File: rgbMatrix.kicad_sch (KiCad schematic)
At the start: 1 part, among them IC1 IS31FL3743A-QULS4-TR

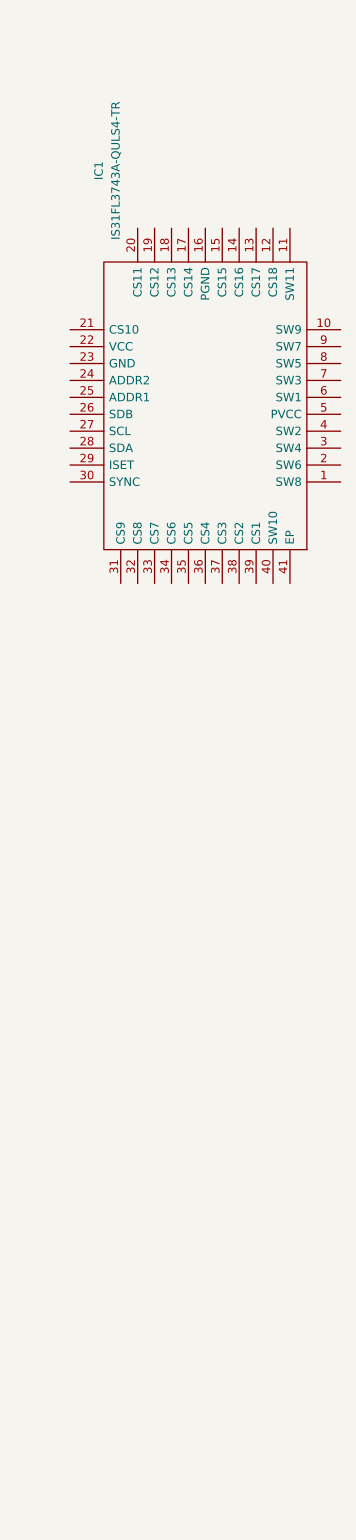
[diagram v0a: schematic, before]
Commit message: Started work on Led sch,
Decided on led driver IC
Decided on led part
started work on led matrix
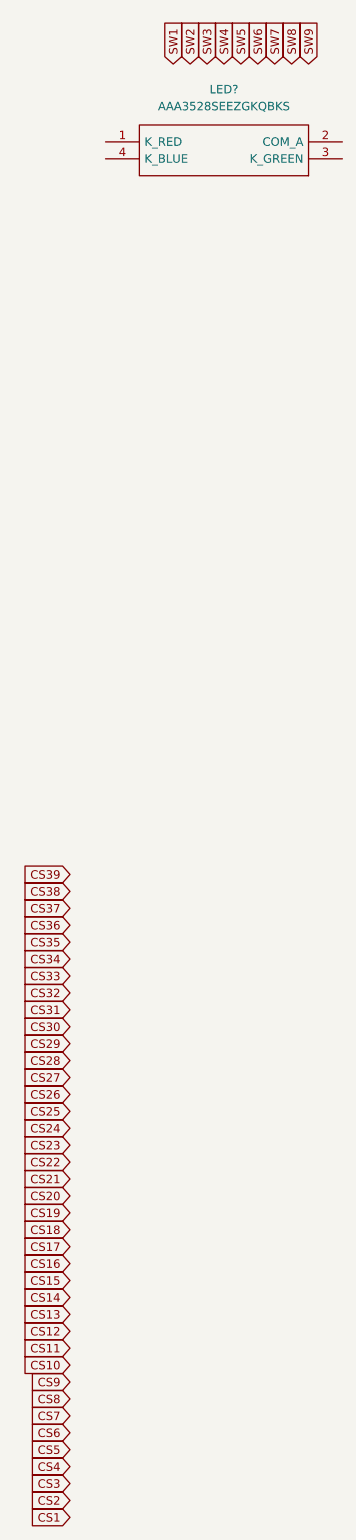
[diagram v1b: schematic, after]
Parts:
- removed IC1: IS31FL3743A-QULS4-TR, QFN40P500X500X60-41N-D, symbol IS31FL3743A-QULS4-TR:IS31FL3743A-QULS4-TR
- added LED?: AAA3528SEEZGKQBKS, AAA3528SEEZGKQBKS, symbol AAA3528SEEZGKQBKS:AAA3528SEEZGKQBKS

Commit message: Changed led driver
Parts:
- added D? (x108): D_Small, symbol Device:D_Small
- added LED? (x116): ESC, AAA3528SEEZGKQBKS, symbol AAA3528SEEZGKQBKS:AAA3528SEEZGKQBKS
- added R_B0, R_B12, R_B? (x11), R_G0, R_G12, R_G? (x11): 20, symbol Device:R_Small
- added R_R0, R_R12, R_R? (x11): 51, symbol Device:R_Small
- added SW?: W, symbol Switch:SW_Push
- added SW? (x3): SW_Push, symbol Switch:SW_Push
- added SW?: R_SHIFT, symbol Switch:SW_Push
- added SW?: 6, symbol Switch:SW_Push
- added SW?: ., symbol Switch:SW_Push
- added SW?: SCR_LK, symbol Switch:SW_Push
- added SW?: /, symbol Switch:SW_Push
- added SW?: X, symbol Switch:SW_Push
- added SW?: PAD_ENTER, symbol Switch:SW_Push
- added SW?: F9, symbol Switch:SW_Push
- added SW?: U, symbol Switch:SW_Push
- added SW?: BACKSPACE, symbol Switch:SW_Push
- added SW?: INSERT, symbol Switch:SW_Push
- added SW?: R_ARROW, symbol Switch:SW_Push
- added SW?: PAD_0, symbol Switch:SW_Push
- added SW?: F12, symbol Switch:SW_Push
- added SW?: 5, symbol Switch:SW_Push
- added SW?: CAPS, symbol Switch:SW_Push
- added SW?: T, symbol Switch:SW_Push
- added SW?: PAD_., symbol Switch:SW_Push
- added SW?: PG_UP, symbol Switch:SW_Push
- added SW?: 9, symbol Switch:SW_Push
- added SW?: ESC, symbol Switch:SW_Push
- added SW?: PAD_8, symbol Switch:SW_Push
- added SW?: F6, symbol Switch:SW_Push
- added SW?: PAD_2, symbol Switch:SW_Push
- added SW?: PAD_5, symbol Switch:SW_Push
- added SW?: +, symbol Switch:SW_Push
- added SW?: PAD_/, symbol Switch:SW_Push
- added SW?: 1, symbol Switch:SW_Push
- added SW?: F11, symbol Switch:SW_Push
- added SW?: I, symbol Switch:SW_Push
- added SW?: Z, symbol Switch:SW_Push
- added SW?: G, symbol Switch:SW_Push
- added SW?: \, symbol Switch:SW_Push
- added SW?: -, symbol Switch:SW_Push
- added SW?: 8, symbol Switch:SW_Push
- added SW?: PAD_BACK, symbol Switch:SW_Push
- added SW?: PAD_1, symbol Switch:SW_Push
- added SW?: E, symbol Switch:SW_Push
- added SW?: PG_DN, symbol Switch:SW_Push
- added SW?: END, symbol Switch:SW_Push
- added SW?: ', symbol Switch:SW_Push
- added SW?: P, symbol Switch:SW_Push
- added SW?: TILDE, symbol Switch:SW_Push
- added SW?: D, symbol Switch:SW_Push
- added SW?: PAD_9, symbol Switch:SW_Push
- added SW?: K, symbol Switch:SW_Push
- added SW?: PAD_3, symbol Switch:SW_Push
- added SW?: 0, symbol Switch:SW_Push
- added SW?: OS, symbol Switch:SW_Push
- added SW?: ENTER, symbol Switch:SW_Push
- added SW?: NUM_LK, symbol Switch:SW_Push
- added SW?: F8, symbol Switch:SW_Push
- added SW?: ], symbol Switch:SW_Push
- added SW?: ;, symbol Switch:SW_Push
- added SW?: =, symbol Switch:SW_Push
- added SW?: *, symbol Switch:SW_Push
- added SW?: F1, symbol Switch:SW_Push
- added SW?: C, symbol Switch:SW_Push
- added SW?: F10, symbol Switch:SW_Push
- added SW?: V, symbol Switch:SW_Push
- added SW?: F4, symbol Switch:SW_Push
- added SW?: PAUSE, symbol Switch:SW_Push
- added SW?: R_ALT, symbol Switch:SW_Push
- added SW?: CTRL, symbol Switch:SW_Push
- added SW?: FN, symbol Switch:SW_Push
- added SW?: 2, symbol Switch:SW_Push
- added SW?: A, symbol Switch:SW_Push
- added SW?: HOME, symbol Switch:SW_Push
- added SW?: R_CTRL, symbol Switch:SW_Push
- added SW?: F3, symbol Switch:SW_Push
- added SW?: PAD_7, symbol Switch:SW_Push
- added SW?: F7, symbol Switch:SW_Push
- added SW?: Y, symbol Switch:SW_Push
- added SW?: [, symbol Switch:SW_Push
- added SW?: PAD_4, symbol Switch:SW_Push
- added SW?: B, symbol Switch:SW_Push
- added SW?: Q, symbol Switch:SW_Push
- added SW?: MENU, symbol Switch:SW_Push
- added SW?: M, symbol Switch:SW_Push
- added SW?: N, symbol Switch:SW_Push
- added SW?: F2, symbol Switch:SW_Push
- added SW?: J, symbol Switch:SW_Push
- added SW?: 7, symbol Switch:SW_Push
- added SW?: F, symbol Switch:SW_Push
- added SW?: H, symbol Switch:SW_Push
- added SW?: PAD_-, symbol Switch:SW_Push
- added SW?: TAB, symbol Switch:SW_Push
- added SW?: 3, symbol Switch:SW_Push
- added SW?: 4, symbol Switch:SW_Push
- added SW?: L, symbol Switch:SW_Push
- added SW?: PRT_SC, symbol Switch:SW_Push
- added SW?: DEL, symbol Switch:SW_Push
- added SW?: DN_ARROW, symbol Switch:SW_Push
- added SW?: PAD_6, symbol Switch:SW_Push
- added SW?: R, symbol Switch:SW_Push
- added SW?: SPACE, symbol Switch:SW_Push
- added SW?: UP_ARROW, symbol Switch:SW_Push
- added SW?: ,, symbol Switch:SW_Push
- added SW?: S, symbol Switch:SW_Push
- added SW?: L_SHIFT, symbol Switch:SW_Push
- added SW?: L_ALT, symbol Switch:SW_Push
- added SW?: L_ARROW, symbol Switch:SW_Push
- added SW?: O, symbol Switch:SW_Push
- added SW?: F5, symbol Switch:SW_Push
- LED?: value AAA3528SEEZGKQBKS -> ESC
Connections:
- net CS1: now also R_G0.1
- net CS10: now also R_G?.1
- net CS11: now also R_R?.1
- net CS12: now also R_B?.1
- net CS13: now also R_G?.1
- net CS14: now also R_R?.1
- net CS15: now also R_B?.1
- net CS16: now also R_G?.1
- net CS17: now also R_R?.1
- net CS18: now also R_B?.1
- net CS19: now also R_G?.1
- net CS2: now also R_R0.1
- net CS20: now also R_R?.1
- net CS21: now also R_B?.1
- net CS22: now also R_G?.1
- net CS23: now also R_R?.1
- net CS24: now also R_B?.1
- net CS25: now also R_G?.1
- net CS26: now also R_R?.1
- net CS27: now also R_B?.1
- net CS28: now also R_G?.1
- net CS29: now also R_R?.1
- net CS3: now also R_B0.1
- net CS30: now also R_B?.1
- net CS31: now also R_G?.1
- net CS32: now also R_R?.1
- net CS33: now also R_B?.1
- net CS34: now also R_G?.1
- net CS35: now also R_R?.1
- net CS36: now also R_B?.1
- net CS37: now also R_G12.1
- net CS38: now also R_R12.1
- net CS39: now also R_B12.1
- net CS4: now also R_G?.1
- net CS5: now also R_R?.1
- net CS6: now also R_B?.1
- net CS7: now also R_G?.1
- net CS8: now also R_R?.1
- net CS9: now also R_B?.1
- net SW1: now also LED?.2 (COM_A), LED?.2 (COM_A), LED?.2 (COM_A), LED?.2 (COM_A), LED?.2 (COM_A), LED?.2 (COM_A), LED?.2 (COM_A), LED?.2 (COM_A), LED?.2 (COM_A), LED?.2 (COM_A), LED?.2 (COM_A), LED?.2 (COM_A), LED?.2 (COM_A), LED?.2 (COM_A), LED?.2 (COM_A), LED?.2 (COM_A), LED?.2 (COM_A)
- net SW2: now also LED?.2 (COM_A), LED?.2 (COM_A), LED?.2 (COM_A), LED?.2 (COM_A), LED?.2 (COM_A), LED?.2 (COM_A), LED?.2 (COM_A), LED?.2 (COM_A), LED?.2 (COM_A), LED?.2 (COM_A), LED?.2 (COM_A), LED?.2 (COM_A), LED?.2 (COM_A), LED?.2 (COM_A), LED?.2 (COM_A), LED?.2 (COM_A), LED?.2 (COM_A), LED?.2 (COM_A), LED?.2 (COM_A), LED?.2 (COM_A), LED?.2 (COM_A)
- net SW3: now also LED?.2 (COM_A), LED?.2 (COM_A), LED?.2 (COM_A), LED?.2 (COM_A), LED?.2 (COM_A), LED?.2 (COM_A), LED?.2 (COM_A), LED?.2 (COM_A), LED?.2 (COM_A), LED?.2 (COM_A), LED?.2 (COM_A), LED?.2 (COM_A), LED?.2 (COM_A), LED?.2 (COM_A), LED?.2 (COM_A), LED?.2 (COM_A), LED?.2 (COM_A), LED?.2 (COM_A), LED?.2 (COM_A), LED?.2 (COM_A), LED?.2 (COM_A)
- net SW4: now also LED?.2 (COM_A), LED?.2 (COM_A), LED?.2 (COM_A), LED?.2 (COM_A), LED?.2 (COM_A), LED?.2 (COM_A), LED?.2 (COM_A), LED?.2 (COM_A), LED?.2 (COM_A), LED?.2 (COM_A), LED?.2 (COM_A), LED?.2 (COM_A), LED?.2 (COM_A), LED?.2 (COM_A), LED?.2 (COM_A), LED?.2 (COM_A), LED?.2 (COM_A), LED?.2 (COM_A)
- net SW5: now also LED?.2 (COM_A), LED?.2 (COM_A), LED?.2 (COM_A), LED?.2 (COM_A), LED?.2 (COM_A), LED?.2 (COM_A), LED?.2 (COM_A), LED?.2 (COM_A), LED?.2 (COM_A), LED?.2 (COM_A), LED?.2 (COM_A), LED?.2 (COM_A), LED?.2 (COM_A), LED?.2 (COM_A), LED?.2 (COM_A), LED?.2 (COM_A), LED?.2 (COM_A), LED?.2 (COM_A), LED?.2 (COM_A)
- net SW6: now also LED?.2 (COM_A), LED?.2 (COM_A), LED?.2 (COM_A), LED?.2 (COM_A), LED?.2 (COM_A), LED?.2 (COM_A), LED?.2 (COM_A), LED?.2 (COM_A), LED?.2 (COM_A), LED?.2 (COM_A), LED?.2 (COM_A), LED?.2 (COM_A), LED?.2 (COM_A), LED?.2 (COM_A), LED?.2 (COM_A), LED?.2 (COM_A), LED?.2 (COM_A), LED?.2 (COM_A), LED?.2 (COM_A), LED?.2 (COM_A), LED?.2 (COM_A)
- net at LED?.1 (K_RED): now also LED?.1 (K_RED), LED?.1 (K_RED), LED?.1 (K_RED), LED?.1 (K_RED), LED?.1 (K_RED), R_B0.2
- net at LED?.3 (K_GREEN): now also LED?.3 (K_GREEN), LED?.3 (K_GREEN), LED?.3 (K_GREEN), LED?.3 (K_GREEN), LED?.3 (K_GREEN), R_G0.2
- net at LED?.4 (K_BLUE): now also LED?.4 (K_BLUE), LED?.4 (K_BLUE), LED?.4 (K_BLUE), LED?.4 (K_BLUE), LED?.4 (K_BLUE), R_R0.2
- new net: D?.2 (A), SW?.1 (x108)
- new net: LED?.1 (K_RED), LED?.1 (K_RED), LED?.1 (K_RED), LED?.1 (K_RED), LED?.1 (K_RED), LED?.1 (K_RED), R_B?.2 (x11)
- new net: LED?.3 (K_GREEN), LED?.3 (K_GREEN), LED?.3 (K_GREEN), LED?.3 (K_GREEN), LED?.3 (K_GREEN), LED?.3 (K_GREEN), R_G?.2 (x11)
- new net: LED?.4 (K_BLUE), LED?.4 (K_BLUE), LED?.4 (K_BLUE), LED?.4 (K_BLUE), LED?.4 (K_BLUE), LED?.4 (K_BLUE), R_R?.2 (x11)
- new net: LED?.1 (K_RED), LED?.1 (K_RED), LED?.1 (K_RED), LED?.1 (K_RED), LED?.1 (K_RED) (x5)
- new net: LED?.3 (K_GREEN), LED?.3 (K_GREEN), LED?.3 (K_GREEN), LED?.3 (K_GREEN), LED?.3 (K_GREEN) (x5)
- new net: LED?.4 (K_BLUE), LED?.4 (K_BLUE), LED?.4 (K_BLUE), LED?.4 (K_BLUE), LED?.4 (K_BLUE) (x5)
- new net: LED?.1 (K_RED), LED?.1 (K_RED), LED?.1 (K_RED), LED?.1 (K_RED), LED?.1 (K_RED), LED?.1 (K_RED)
- new net: LED?.3 (K_GREEN), LED?.3 (K_GREEN), LED?.3 (K_GREEN), LED?.3 (K_GREEN), LED?.3 (K_GREEN), LED?.3 (K_GREEN)
- new net: LED?.4 (K_BLUE), LED?.4 (K_BLUE), LED?.4 (K_BLUE), LED?.4 (K_BLUE), LED?.4 (K_BLUE), LED?.4 (K_BLUE)
- new net: LED?.3 (K_GREEN), LED?.3 (K_GREEN), LED?.3 (K_GREEN), LED?.3 (K_GREEN), LED?.3 (K_GREEN), LED?.3 (K_GREEN), R_G12.2
- new net: LED?.1 (K_RED), LED?.1 (K_RED), LED?.1 (K_RED), LED?.1 (K_RED) (x2)
- new net: LED?.3 (K_GREEN), LED?.3 (K_GREEN), LED?.3 (K_GREEN), LED?.3 (K_GREEN) (x2)
- new net: LED?.4 (K_BLUE), LED?.4 (K_BLUE), LED?.4 (K_BLUE), LED?.4 (K_BLUE) (x2)
- new net: LED?.1 (K_RED), LED?.1 (K_RED), LED?.1 (K_RED), LED?.1 (K_RED), LED?.1 (K_RED), LED?.1 (K_RED), R_B12.2
- new net: LED?.4 (K_BLUE), LED?.4 (K_BLUE), LED?.4 (K_BLUE), LED?.4 (K_BLUE), LED?.4 (K_BLUE), LED?.4 (K_BLUE), R_R12.2
- new net COL0: SW?.2, SW?.2, SW?.2, SW?.2, SW?.2, SW?.2
- new net COL1: SW?.2, SW?.2, SW?.2, SW?.2, SW?.2
- new net COL10: SW?.2, SW?.2, SW?.2, SW?.2, SW?.2, SW?.2
- new net COL11: SW?.2, SW?.2, SW?.2, SW?.2, SW?.2, SW?.2
- new net COL12: SW?.2, SW?.2, SW?.2
- new net COL13: SW?.2, SW?.2, SW?.2, SW?.2, SW?.2
- new net COL14: SW?.2, SW?.2, SW?.2, SW?.2
- new net COL15: SW?.2, SW?.2, SW?.2, SW?.2, SW?.2
- new net COL16: SW?.2, SW?.2, SW?.2, SW?.2
- new net COL17: SW?.2, SW?.2, SW?.2, SW?.2, SW?.2
- new net COL18: SW?.2, SW?.2, SW?.2, SW?.2, SW?.2
- new net COL19: SW?.2, SW?.2, SW?.2, SW?.2, SW?.2
- new net COL2: SW?.2, SW?.2, SW?.2, SW?.2, SW?.2, SW?.2
- new net COL20: SW?.2, SW?.2, SW?.2, SW?.2, SW?.2
- new net COL3: SW?.2, SW?.2, SW?.2, SW?.2, SW?.2
- new net COL4: SW?.2, SW?.2, SW?.2, SW?.2, SW?.2
- new net COL5: SW?.2, SW?.2, SW?.2, SW?.2, SW?.2, SW?.2
- new net COL6: SW?.2, SW?.2, SW?.2, SW?.2, SW?.2
- new net COL7: SW?.2, SW?.2, SW?.2, SW?.2, SW?.2
- new net COL8: SW?.2, SW?.2, SW?.2, SW?.2, SW?.2, SW?.2
- new net COL9: SW?.2, SW?.2, SW?.2, SW?.2, SW?.2, SW?.2
- new net ROW0: D?.1 (K), D?.1 (K), D?.1 (K), D?.1 (K), D?.1 (K), D?.1 (K), D?.1 (K), D?.1 (K), D?.1 (K), D?.1 (K), D?.1 (K), D?.1 (K), D?.1 (K), D?.1 (K), D?.1 (K), D?.1 (K), D?.1 (K)
- new net ROW1: D?.1 (K), D?.1 (K), D?.1 (K), D?.1 (K), D?.1 (K), D?.1 (K), D?.1 (K), D?.1 (K), D?.1 (K), D?.1 (K), D?.1 (K), D?.1 (K), D?.1 (K), D?.1 (K), D?.1 (K), D?.1 (K), D?.1 (K), D?.1 (K), D?.1 (K), D?.1 (K), D?.1 (K)
- new net ROW2: D?.1 (K), D?.1 (K), D?.1 (K), D?.1 (K), D?.1 (K), D?.1 (K), D?.1 (K), D?.1 (K), D?.1 (K), D?.1 (K), D?.1 (K), D?.1 (K), D?.1 (K), D?.1 (K), D?.1 (K), D?.1 (K), D?.1 (K), D?.1 (K), D?.1 (K), D?.1 (K), D?.1 (K)
- new net ROW3: D?.1 (K), D?.1 (K), D?.1 (K), D?.1 (K), D?.1 (K), D?.1 (K), D?.1 (K), D?.1 (K), D?.1 (K), D?.1 (K), D?.1 (K), D?.1 (K), D?.1 (K), D?.1 (K), D?.1 (K), D?.1 (K), D?.1 (K)
- new net ROW4: D?.1 (K), D?.1 (K), D?.1 (K), D?.1 (K), D?.1 (K), D?.1 (K), D?.1 (K), D?.1 (K), D?.1 (K), D?.1 (K), D?.1 (K), D?.1 (K), D?.1 (K), D?.1 (K), D?.1 (K), D?.1 (K), D?.1 (K)
- new net ROW5: D?.1 (K), D?.1 (K), D?.1 (K), D?.1 (K), D?.1 (K), D?.1 (K), D?.1 (K), D?.1 (K), D?.1 (K), D?.1 (K), D?.1 (K), D?.1 (K), D?.1 (K), D?.1 (K), D?.1 (K)
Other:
- moved on the sheet: LED?

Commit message: Finished Electric Schematic Of Keyboard
All components are now wired. Positions for spacers, button stabilizers, and threated holes not accounted.
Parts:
- removed D? (x108): D_Small, symbol Device:D_Small
- removed LED? (x11): ESC, AAA3528SEEZGKQBKS, symbol AAA3528SEEZGKQBKS:AAA3528SEEZGKQBKS
- removed R_B? (x2), R_G? (x2): 20, symbol Device:R_Small
- removed R_R? (x2): 51, symbol Device:R_Small
- removed SW?: W, symbol Switch:SW_Push
- removed SW? (x3): SW_Push, symbol Switch:SW_Push
- removed SW?: R_SHIFT, symbol Switch:SW_Push
- removed SW?: 6, symbol Switch:SW_Push
- removed SW?: ., symbol Switch:SW_Push
- removed SW?: SCR_LK, symbol Switch:SW_Push
- removed SW?: /, symbol Switch:SW_Push
- removed SW?: X, symbol Switch:SW_Push
- removed SW?: PAD_ENTER, symbol Switch:SW_Push
- removed SW?: F9, symbol Switch:SW_Push
- removed SW?: U, symbol Switch:SW_Push
- removed SW?: BACKSPACE, symbol Switch:SW_Push
- removed SW?: INSERT, symbol Switch:SW_Push
- removed SW?: R_ARROW, symbol Switch:SW_Push
- removed SW?: PAD_0, symbol Switch:SW_Push
- removed SW?: F12, symbol Switch:SW_Push
- removed SW?: 5, symbol Switch:SW_Push
- removed SW?: CAPS, symbol Switch:SW_Push
- removed SW?: T, symbol Switch:SW_Push
- removed SW?: PAD_., symbol Switch:SW_Push
- removed SW?: PG_UP, symbol Switch:SW_Push
- removed SW?: 9, symbol Switch:SW_Push
- removed SW?: ESC, symbol Switch:SW_Push
- removed SW?: PAD_8, symbol Switch:SW_Push
- removed SW?: F6, symbol Switch:SW_Push
- removed SW?: PAD_2, symbol Switch:SW_Push
- removed SW?: PAD_5, symbol Switch:SW_Push
- removed SW?: +, symbol Switch:SW_Push
- removed SW?: PAD_/, symbol Switch:SW_Push
- removed SW?: 1, symbol Switch:SW_Push
- removed SW?: F11, symbol Switch:SW_Push
- removed SW?: I, symbol Switch:SW_Push
- removed SW?: Z, symbol Switch:SW_Push
- removed SW?: G, symbol Switch:SW_Push
- removed SW?: \, symbol Switch:SW_Push
- removed SW?: -, symbol Switch:SW_Push
- removed SW?: 8, symbol Switch:SW_Push
- removed SW?: PAD_BACK, symbol Switch:SW_Push
- removed SW?: PAD_1, symbol Switch:SW_Push
- removed SW?: E, symbol Switch:SW_Push
- removed SW?: PG_DN, symbol Switch:SW_Push
- removed SW?: END, symbol Switch:SW_Push
- removed SW?: ', symbol Switch:SW_Push
- removed SW?: P, symbol Switch:SW_Push
- removed SW?: TILDE, symbol Switch:SW_Push
- removed SW?: D, symbol Switch:SW_Push
- removed SW?: PAD_9, symbol Switch:SW_Push
- removed SW?: K, symbol Switch:SW_Push
- removed SW?: PAD_3, symbol Switch:SW_Push
- removed SW?: 0, symbol Switch:SW_Push
- removed SW?: OS, symbol Switch:SW_Push
- removed SW?: ENTER, symbol Switch:SW_Push
- removed SW?: NUM_LK, symbol Switch:SW_Push
- removed SW?: F8, symbol Switch:SW_Push
- removed SW?: ], symbol Switch:SW_Push
- removed SW?: ;, symbol Switch:SW_Push
- removed SW?: =, symbol Switch:SW_Push
- removed SW?: *, symbol Switch:SW_Push
- removed SW?: F1, symbol Switch:SW_Push
- removed SW?: C, symbol Switch:SW_Push
- removed SW?: F10, symbol Switch:SW_Push
- removed SW?: V, symbol Switch:SW_Push
- removed SW?: F4, symbol Switch:SW_Push
- removed SW?: PAUSE, symbol Switch:SW_Push
- removed SW?: R_ALT, symbol Switch:SW_Push
- removed SW?: CTRL, symbol Switch:SW_Push
- removed SW?: FN, symbol Switch:SW_Push
- removed SW?: 2, symbol Switch:SW_Push
- removed SW?: A, symbol Switch:SW_Push
- removed SW?: HOME, symbol Switch:SW_Push
- removed SW?: R_CTRL, symbol Switch:SW_Push
- removed SW?: F3, symbol Switch:SW_Push
- removed SW?: PAD_7, symbol Switch:SW_Push
- removed SW?: F7, symbol Switch:SW_Push
- removed SW?: Y, symbol Switch:SW_Push
- removed SW?: [, symbol Switch:SW_Push
- removed SW?: PAD_4, symbol Switch:SW_Push
- removed SW?: B, symbol Switch:SW_Push
- removed SW?: Q, symbol Switch:SW_Push
- removed SW?: MENU, symbol Switch:SW_Push
- removed SW?: M, symbol Switch:SW_Push
- removed SW?: N, symbol Switch:SW_Push
- removed SW?: F2, symbol Switch:SW_Push
- removed SW?: J, symbol Switch:SW_Push
- removed SW?: 7, symbol Switch:SW_Push
- removed SW?: F, symbol Switch:SW_Push
- removed SW?: H, symbol Switch:SW_Push
- removed SW?: PAD_-, symbol Switch:SW_Push
- removed SW?: TAB, symbol Switch:SW_Push
- removed SW?: 3, symbol Switch:SW_Push
- removed SW?: 4, symbol Switch:SW_Push
- removed SW?: L, symbol Switch:SW_Push
- removed SW?: PRT_SC, symbol Switch:SW_Push
- removed SW?: DEL, symbol Switch:SW_Push
- removed SW?: DN_ARROW, symbol Switch:SW_Push
- removed SW?: PAD_6, symbol Switch:SW_Push
- removed SW?: R, symbol Switch:SW_Push
- removed SW?: SPACE, symbol Switch:SW_Push
- removed SW?: UP_ARROW, symbol Switch:SW_Push
- removed SW?: ,, symbol Switch:SW_Push
- removed SW?: S, symbol Switch:SW_Push
- removed SW?: L_SHIFT, symbol Switch:SW_Push
- removed SW?: L_ALT, symbol Switch:SW_Push
- removed SW?: L_ARROW, symbol Switch:SW_Push
- removed SW?: O, symbol Switch:SW_Push
- removed SW?: F5, symbol Switch:SW_Push
- added R_B11, R_B12, R_B14, R_B15, R_B16, R_B17, R_B18, R_B19, R_B20, R_G11, R_G12, R_G14, R_G15, R_G16, R_G17, R_G18, R_G19, R_G20: 20, symbol Device:R_Small
- added R_R11, R_R12, R_R14, R_R15, R_R16, R_R17, R_R18, R_R19, R_R20: 51, symbol Device:R_Small
- LED10: renamed from LED?; value ESC -> F9
- LED100: renamed from LED?; value ESC -> R_CTRL
- LED101: renamed from LED?; value ESC -> L_ARROW
- LED102: renamed from LED?; value ESC -> DN_ARROW
- LED103: renamed from LED?; value ESC -> R_ARROW
- LED104: renamed from LED?; value ESC -> PAD_0
- LED105, LED84: renamed from LED?; value ESC -> .
- LED106: renamed from LED?; value ESC -> PAD_ENTER
- LED11: renamed from LED?; value ESC -> F10
- LED12: renamed from LED?; value ESC -> F11
- LED13: renamed from LED?; value ESC -> F12
- LED14: renamed from LED?; value ESC -> PRT_SC
- LED15: renamed from LED?; value ESC -> SCR_LK
- LED16: renamed from LED?; value ESC -> PAUSE
- LED17: renamed from LED?; value ESC -> TILDE
- LED18: renamed from LED?; value ESC -> 1
- LED19: renamed from LED?; value ESC -> 2
- LED2: renamed from LED?; value ESC -> F1
- LED20: renamed from LED?; value ESC -> 3
- LED21: renamed from LED?; value ESC -> 4
- LED22: renamed from LED?; value ESC -> 5
- LED23: renamed from LED?; value ESC -> 6
- LED24: renamed from LED?; value ESC -> 7
- LED25: renamed from LED?; value ESC -> 8
- LED26: renamed from LED?; value ESC -> 9
- LED27: renamed from LED?; value ESC -> 0
- LED28: renamed from LED?; value ESC -> -
- LED29: renamed from LED?; value ESC -> =
- LED3: renamed from LED?; value ESC -> F2
- LED30: renamed from LED?; value ESC -> BACKSPACE
- LED31: renamed from LED?; value ESC -> INSERT
- LED32: renamed from LED?; value ESC -> HOME
- LED33: renamed from LED?; value ESC -> PG_UP
- LED34: renamed from LED?; value ESC -> NUM_LK
- LED35: renamed from LED?; value ESC -> PAD_/
- LED36: renamed from LED?; value ESC -> *
- LED37: renamed from LED?; value ESC -> PAD_-
- LED38: renamed from LED?; value ESC -> TAB
- LED39: renamed from LED?; value ESC -> Q
- LED4: renamed from LED?; value ESC -> F3
- LED40: renamed from LED?; value ESC -> W
- LED41: renamed from LED?; value ESC -> E
- LED42: renamed from LED?; value ESC -> R
- LED43: renamed from LED?; value ESC -> T
- LED44: renamed from LED?; value ESC -> Y
- LED45: renamed from LED?; value ESC -> U
- LED46: renamed from LED?; value ESC -> I
- LED47: renamed from LED?; value ESC -> O
- LED48: renamed from LED?; value ESC -> P
- LED49: renamed from LED?; value ESC -> [
- LED5: renamed from LED?; value ESC -> F4
- LED50: renamed from LED?; value ESC -> ]
- LED51: renamed from LED?; value ESC -> \
- LED52: renamed from LED?; value ESC -> DEL
- LED53: renamed from LED?; value ESC -> END
- LED54: renamed from LED?; value ESC -> PG_DN
- LED55: renamed from LED?; value ESC -> PAD_7
- LED56: renamed from LED?; value ESC -> PAD_8
- LED57: renamed from LED?; value ESC -> PAD_9
- LED58: renamed from LED?; value ESC -> +
- LED59: renamed from LED?; value ESC -> CAPS
- LED6: renamed from LED?; value ESC -> F5
- LED60: renamed from LED?; value ESC -> A
- LED61: renamed from LED?; value ESC -> S
- LED62: renamed from LED?; value ESC -> D
- LED63: renamed from LED?; value ESC -> F
- LED64: renamed from LED?; value ESC -> G
- LED65: renamed from LED?; value ESC -> H
- LED66: renamed from LED?; value ESC -> J
- LED67: renamed from LED?; value ESC -> K
- LED68: renamed from LED?; value ESC -> L
- LED69: renamed from LED?; value ESC -> ;
- LED7: renamed from LED?; value ESC -> F6
- LED70: renamed from LED?; value ESC -> '
- LED71: renamed from LED?; value ESC -> ENTER
- LED72: renamed from LED?; value ESC -> PAD_4
- LED73: renamed from LED?; value ESC -> PAD_5
- LED74: renamed from LED?; value ESC -> PAD_6
- LED75: renamed from LED?; value ESC -> L_SHIFT
- LED76: renamed from LED?; value ESC -> Z
- LED77: renamed from LED?; value ESC -> X
- LED78: renamed from LED?; value ESC -> C
- LED79: renamed from LED?; value ESC -> V
- LED8: renamed from LED?; value ESC -> F7
- LED80: renamed from LED?; value ESC -> B
- LED81: renamed from LED?; value ESC -> N
- LED82: renamed from LED?; value ESC -> M
- LED83: renamed from LED?; value ESC -> ,
- LED85: renamed from LED?; value ESC -> /
- LED86: renamed from LED?; value ESC -> R_SHIFT
- LED87: renamed from LED?; value ESC -> UP_ARROW
- LED88: renamed from LED?; value ESC -> PAD_1
- LED89: renamed from LED?; value ESC -> PAD_2
- LED9: renamed from LED?; value ESC -> F8
- LED90: renamed from LED?; value ESC -> PAD_3
- LED91: renamed from LED?; value ESC -> CTRL
- LED92: renamed from LED?; value ESC -> OS
- LED93: renamed from LED?; value ESC -> L_ALT
- LED94: renamed from LED?; value ESC -> SPACE_L
- LED95: renamed from LED?; value ESC -> SPACE
- LED96: renamed from LED?; value ESC -> SPACE_R
- LED97: renamed from LED?; value ESC -> R_ALT
- LED98: renamed from LED?; value ESC -> FN
- LED99: renamed from LED?; value ESC -> MENU
- gave numbers to parts that had none: 28
- renumbered R_B0 to R_B1, R_B12 to R_B13, R_G0 to R_G1, R_G12 to R_G13, R_R0 to R_R1, R_R12 to R_R13
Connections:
- net CS31: now also R_G11.1
- net CS32: now also R_R11.1
- net CS33: now also R_B11.1
- net CS34: now also R_G12.1
- net CS35: now also R_R12.1
- net CS36: now also R_B12.1
- net SW1: no longer LED10.2 (COM_A), LED11.2 (COM_A), LED12.2 (COM_A), LED13.2 (COM_A), LED14.2 (COM_A), LED15.2 (COM_A), LED16.2 (COM_A)
- net SW2: no longer LED27.2 (COM_A), LED28.2 (COM_A), LED29.2 (COM_A), LED30.2 (COM_A), LED31.2 (COM_A), LED32.2 (COM_A), LED33.2 (COM_A), LED34.2 (COM_A), LED35.2 (COM_A), LED36.2 (COM_A), LED37.2 (COM_A)
- net SW3: no longer LED48.2 (COM_A), LED49.2 (COM_A), LED50.2 (COM_A), LED51.2 (COM_A), LED52.2 (COM_A), LED53.2 (COM_A), LED54.2 (COM_A), LED55.2 (COM_A), LED56.2 (COM_A), LED57.2 (COM_A), LED58.2 (COM_A)
- net SW4: no longer LED69.2 (COM_A), LED70.2 (COM_A), LED71.2 (COM_A), LED72.2 (COM_A), LED73.2 (COM_A), LED74.2 (COM_A)
- net SW5: no longer LED84.2 (COM_A), LED85.2 (COM_A), LED86.2 (COM_A), LED87.2 (COM_A), LED88.2 (COM_A), LED89.2 (COM_A), LED90.2 (COM_A)
- net SW6: no longer LED100.2 (COM_A), LED101.2 (COM_A), LED102.2 (COM_A), LED103.2 (COM_A), LED104.2 (COM_A), LED105.2 (COM_A), LED106.2 (COM_A), LED99.2 (COM_A)
- net SW7: now also LED10.2 (COM_A), LED11.2 (COM_A), LED12.2 (COM_A), LED13.2 (COM_A), LED15.2 (COM_A), LED16.2 (COM_A), LED34.2 (COM_A)
- net SW8: now also LED27.2 (COM_A), LED28.2 (COM_A), LED29.2 (COM_A), LED30.2 (COM_A), LED32.2 (COM_A), LED33.2 (COM_A), LED35.2 (COM_A), LED36.2 (COM_A), LED37.2 (COM_A), LED55.2 (COM_A)
- net SW9: now also LED48.2 (COM_A), LED49.2 (COM_A), LED50.2 (COM_A), LED51.2 (COM_A), LED53.2 (COM_A), LED54.2 (COM_A), LED56.2 (COM_A), LED57.2 (COM_A), LED58.2 (COM_A), LED72.2 (COM_A)
- net at LED15.1 (K_RED), LED32.1 (K_RED), LED53.1 (K_RED): now also LED14.1 (K_RED), LED31.1 (K_RED), LED52.1 (K_RED), R_B15.2; no longer LED102.1 (K_RED), LED87.1 (K_RED)
- net at LED15.3 (K_GREEN), LED32.3 (K_GREEN), LED53.3 (K_GREEN): now also LED14.3 (K_GREEN), LED31.3 (K_GREEN), LED52.3 (K_GREEN), R_G15.2; no longer LED102.3 (K_GREEN), LED87.3 (K_GREEN)
- net at LED15.4 (K_BLUE), LED32.4 (K_BLUE), LED53.4 (K_BLUE): now also LED14.4 (K_BLUE), LED31.4 (K_BLUE), LED52.4 (K_BLUE), R_R15.2; no longer LED102.4 (K_BLUE), LED87.4 (K_BLUE)
- net at LED105.1 (K_RED), LED35.1 (K_RED), LED56.1 (K_RED)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: now also R_B18.2
- net at LED105.3 (K_GREEN), LED35.3 (K_GREEN), LED56.3 (K_GREEN)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: now also R_G18.2
- net at LED105.4 (K_BLUE), LED35.4 (K_BLUE), LED56.4 (K_BLUE)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: now also R_R18.2
- net at LED104.1 (K_RED), LED34.1 (K_RED), LED55.1 (K_RED)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: now also LED103.1 (K_RED), R_B17.2
- net at LED104.3 (K_GREEN), LED34.3 (K_GREEN), LED55.3 (K_GREEN)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: now also LED103.3 (K_GREEN), R_G17.2
- net at LED104.4 (K_BLUE), LED34.4 (K_BLUE), LED55.4 (K_BLUE)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: now also LED103.4 (K_BLUE), R_R17.2
- net at LED106.1 (K_RED), LED37.1 (K_RED), LED58.1 (K_RED): now also R_B20.2
- net at LED106.3 (K_GREEN), LED37.3 (K_GREEN), LED58.3 (K_GREEN): now also R_G20.2
- net at LED106.4 (K_BLUE), LED37.4 (K_BLUE), LED58.4 (K_BLUE): now also R_R20.2
- net at LED13.1 (K_RED), LED30.1 (K_RED), LED51.1 (K_RED)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: now also R_B14.2
- net at LED13.3 (K_GREEN), LED30.3 (K_GREEN), LED51.3 (K_GREEN)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: now also R_G14.2
- net at LED13.4 (K_BLUE), LED30.4 (K_BLUE), LED51.4 (K_BLUE)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: now also R_R14.2
- net at LED10.1 (K_RED), LED27.1 (K_RED), LED48.1 (K_RED)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: now also R_B11.2
- net at LED10.3 (K_GREEN), LED27.3 (K_GREEN), LED48.3 (K_GREEN)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: now also R_G11.2
- net at LED10.4 (K_BLUE), LED27.4 (K_BLUE), LED48.4 (K_BLUE)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: now also R_R11.2
- net at LED100.1 (K_RED), LED11.1 (K_RED), LED28.1 (K_RED)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: now also R_B12.2
- net at LED100.3 (K_GREEN), LED11.3 (K_GREEN), LED28.3 (K_GREEN)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: now also R_G12.2
- net at LED100.4 (K_BLUE), LED11.4 (K_BLUE), LED28.4 (K_BLUE)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: now also R_R12.2
- net at LED16.1 (K_RED), LED33.1 (K_RED), LED54.1 (K_RED): now also LED101.1 (K_RED), LED102.1 (K_RED), LED87.1 (K_RED), R_B16.2; no longer LED103.1 (K_RED)
- net at LED16.3 (K_GREEN), LED33.3 (K_GREEN), LED54.3 (K_GREEN): now also LED101.3 (K_GREEN), LED102.3 (K_GREEN), LED87.3 (K_GREEN), R_G16.2; no longer LED103.3 (K_GREEN)
- net at LED16.4 (K_BLUE), LED33.4 (K_BLUE), LED54.4 (K_BLUE): now also LED101.4 (K_BLUE), LED102.4 (K_BLUE), LED87.4 (K_BLUE), R_R16.2; no longer LED103.4 (K_BLUE)
- net at LED36.1 (K_RED), LED57.1 (K_RED), LED74.1 (K_RED)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: now also R_B19.2
- net at LED36.3 (K_GREEN), LED57.3 (K_GREEN), LED74.3 (K_GREEN)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: now also R_G19.2
- net at LED36.4 (K_BLUE), LED57.4 (K_BLUE), LED74.4 (K_BLUE)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: now also R_R19.2
- new net CS40: R_G14.1
- new net CS41: R_R14.1
- new net CS42: R_B14.1
- new net CS43: R_G15.1
- new net CS44: R_R15.1
- new net CS45: R_B15.1
- new net CS46: R_G16.1
- new net CS47: R_R16.1
- new net CS48: R_B16.1
- new net CS49: R_G17.1
- new net CS50: R_R17.1
- new net CS51: R_B17.1
- new net CS52: R_G18.1
- new net CS53: R_R18.1
- new net CS54: R_B18.1
- new net CS55: R_G19.1
- new net CS56: R_R19.1
- new net CS57: R_B19.1
- new net CS58: R_G20.1
- new net CS59: R_R20.1
- new net CS60: R_B20.1
- new net SW10: LED14.2 (COM_A), LED69.2 (COM_A), LED70.2 (COM_A), LED71.2 (COM_A), LED73.2 (COM_A), LED74.2 (COM_A), LED87.2 (COM_A), LED88.2 (COM_A)
- new net SW11: LED102.2 (COM_A), LED104.2 (COM_A), LED31.2 (COM_A), LED84.2 (COM_A), LED85.2 (COM_A), LED86.2 (COM_A), LED89.2 (COM_A), LED90.2 (COM_A)
- new net SW12: LED100.2 (COM_A), LED101.2 (COM_A), LED103.2 (COM_A), LED105.2 (COM_A), LED106.2 (COM_A), LED52.2 (COM_A), LED99.2 (COM_A)
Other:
- note added: "SW1, COL16"
- note added: "SW2, COL16"
- note added: "SW3, COL16"
- note added: "SW4, COL14"
- note added: "SW4, COL15"
- note added: "SW4, COL16"
- note added: "SW5, COL14"
- note added: "SW5, COL15"
- note added: "SW5, COL16"
- note added: "SW6, COL14"
- note added: "SW6, COL15"
- note added: "SW6, COL16"
- moved on the sheet: LED10, LED100, LED101, LED102, LED103, LED104, LED105, LED106, LED11, LED12, LED13, LED14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

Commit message: Started work on PCB layout
Slightly Adjusted electric schematic as well.
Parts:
- LED1, LED10, LED100, LED101, LED102, LED103, LED104, LED106, LED11, LED12, LED13, LED14, LED15, LED16, LED17, LED18, LED19, LED2, LED20, LED21, LED22, LED23, LED24, LED25, LED26, LED27, LED28, LED29, LED3, LED30, LED31, LED32, LED33, LED34, LED35, LED36, LED37, LED38, LED39, LED4, LED40, LED41, LED42, LED43, LED44, LED45, LED46, LED47, LED48, LED49, LED5, LED50, LED51, LED52, LED53, LED54, LED55, LED56, LED57, LED58, LED59, LED6, LED60, LED61, LED62, LED63, LED64, LED65, LED66, LED67, LED68, LED69, LED7, LED70, LED71, LED72, LED73, LED74, LED75, LED76, LED77, LED78, LED79, LED8, LED80, LED81, LED82, LED83, LED84, LED85, LED86, LED87, LED88, LED89, LED9, LED90, LED91, LED92, LED93, LED94, LED95, LED96, LED97, LED98, LED99: footprint AAA3528SEEZGKQBKS -> mouser_AAA3528SEEZGKQBKS:AAA3528SEEZGKQBKS
- LED105: value . -> PAD_.; footprint AAA3528SEEZGKQBKS -> mouser_AAA3528SEEZGKQBKS:AAA3528SEEZGKQBKS
- R_B1, R_B10, R_B11, R_B12, R_B13, R_B14, R_B15, R_B16, R_B17, R_B18, R_B19, R_B2, R_B20, R_B3, R_B4, R_B5, R_B6, R_B7, R_B8, R_B9, R_G1, R_G10, R_G11, R_G12, R_G13, R_G14, R_G15, R_G16, R_G17, R_G18, R_G19, R_G2, R_G20, R_G3, R_G4, R_G5, R_G6, R_G7, R_G8, R_G9, R_R1, R_R10, R_R11, R_R12, R_R13, R_R14, R_R15, R_R16, R_R17, R_R18, R_R19, R_R2, R_R20, R_R3, R_R4, R_R5, R_R6, R_R7, R_R8, R_R9: footprint (none) -> Resistor_SMD:R_0805_2012Metric_Pad1.20x1.40mm_HandSolder
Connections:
- net SW10: now also LED72.2 (COM_A); no longer LED14.2 (COM_A), LED87.2 (COM_A), LED88.2 (COM_A)
- net SW11: now also LED87.2 (COM_A), LED88.2 (COM_A); no longer LED102.2 (COM_A), LED104.2 (COM_A), LED31.2 (COM_A)
- net SW12: now also LED102.2 (COM_A), LED104.2 (COM_A); no longer LED52.2 (COM_A)
- net SW7: now also LED14.2 (COM_A), LED36.2 (COM_A), LED37.2 (COM_A); no longer LED34.2 (COM_A)
- net SW8: now also LED31.2 (COM_A), LED34.2 (COM_A), LED58.2 (COM_A); no longer LED36.2 (COM_A), LED37.2 (COM_A), LED55.2 (COM_A)
- net SW9: now also LED52.2 (COM_A), LED55.2 (COM_A); no longer LED58.2 (COM_A), LED72.2 (COM_A)
- net at LED57.1 (K_RED), LED74.1 (K_RED), LED90.1 (K_RED): now also LED106.1 (K_RED), LED37.1 (K_RED), LED58.1 (K_RED), R_B20.2; no longer LED36.1 (K_RED), R_B19.2
- net at LED14.1 (K_RED), LED31.1 (K_RED), LED52.1 (K_RED)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: now also LED101.1 (K_RED); no longer LED15.1 (K_RED), LED32.1 (K_RED), LED53.1 (K_RED)
- net at LED14.3 (K_GREEN), LED31.3 (K_GREEN), LED52.3 (K_GREEN)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: now also LED101.3 (K_GREEN); no longer LED15.3 (K_GREEN), LED32.3 (K_GREEN), LED53.3 (K_GREEN)
- net at LED14.4 (K_BLUE), LED31.4 (K_BLUE), LED52.4 (K_BLUE)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: now also LED101.4 (K_BLUE); no longer LED15.4 (K_BLUE), LED32.4 (K_BLUE), LED53.4 (K_BLUE)
- net at LED105.1 (K_RED), LED35.1 (K_RED), LED56.1 (K_RED)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: now also LED36.1 (K_RED), R_B19.2; no longer R_B18.2
- net at LED105.3 (K_GREEN), LED35.3 (K_GREEN), LED56.3 (K_GREEN)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: now also LED36.3 (K_GREEN), R_G19.2; no longer R_G18.2
- net at LED105.4 (K_BLUE), LED35.4 (K_BLUE), LED56.4 (K_BLUE)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: now also LED36.4 (K_BLUE), R_R19.2; no longer R_R18.2
- net at LED104.1 (K_RED), LED34.1 (K_RED), LED55.1 (K_RED)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: now also R_B18.2; no longer LED103.1 (K_RED), R_B17.2
- net at LED104.3 (K_GREEN), LED34.3 (K_GREEN), LED55.3 (K_GREEN)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: now also R_G18.2; no longer LED103.3 (K_GREEN), R_G17.2
- net at LED104.4 (K_BLUE), LED34.4 (K_BLUE), LED55.4 (K_BLUE)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: now also R_R18.2; no longer LED103.4 (K_BLUE), R_R17.2
- net at LED57.4 (K_BLUE), LED74.4 (K_BLUE), LED90.4 (K_BLUE): now also LED106.4 (K_BLUE), LED37.4 (K_BLUE), LED58.4 (K_BLUE), R_R20.2; no longer LED36.4 (K_BLUE), R_R19.2
- net at LED106.3 (K_GREEN), LED37.3 (K_GREEN), LED58.3 (K_GREEN)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: now also LED57.3 (K_GREEN), LED74.3 (K_GREEN), LED90.3 (K_GREEN)
- new net: LED102.1 (K_RED), LED15.1 (K_RED), LED32.1 (K_RED), LED53.1 (K_RED), LED87.1 (K_RED), R_B16.2
- new net: LED102.3 (K_GREEN), LED15.3 (K_GREEN), LED32.3 (K_GREEN), LED53.3 (K_GREEN), LED87.3 (K_GREEN), R_G16.2
- new net: LED102.4 (K_BLUE), LED15.4 (K_BLUE), LED32.4 (K_BLUE), LED53.4 (K_BLUE), LED87.4 (K_BLUE), R_R16.2
- new net: LED103.3 (K_GREEN), LED16.3 (K_GREEN), LED33.3 (K_GREEN), LED54.3 (K_GREEN), R_G17.2
- new net: LED103.4 (K_BLUE), LED16.4 (K_BLUE), LED33.4 (K_BLUE), LED54.4 (K_BLUE), R_R17.2
- new net: LED103.1 (K_RED), LED16.1 (K_RED), LED33.1 (K_RED), LED54.1 (K_RED), R_B17.2
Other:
- note added: "SW10, COL 20"
- note added: "SW11 COL 20"
- note added: "SW12, COL 20"
- note added: "SW7, COL 19"
- note added: "SW7, COL 20"
- note added: "SW8, COL 20"
- note added: "SW9, COL 20"
- note removed: "SW1, COL16"
- note removed: "SW2, COL16"
- note removed: "SW3, COL16"
- note removed: "SW4, COL14"
- note removed: "SW4, COL15"
- note removed: "SW4, COL16"
- note removed: "SW5, COL14"
- note removed: "SW5, COL15"
- note removed: "SW5, COL16"
- note removed: "SW6, COL14"
- note removed: "SW6, COL15"
- note removed: "SW6, COL16"
- moved on the sheet: LED10, LED100, LED101, LED102, LED103, LED104, LED105, LED106, LED11, LED12, LED13, LED14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
